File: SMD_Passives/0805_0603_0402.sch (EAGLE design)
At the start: 5 parts

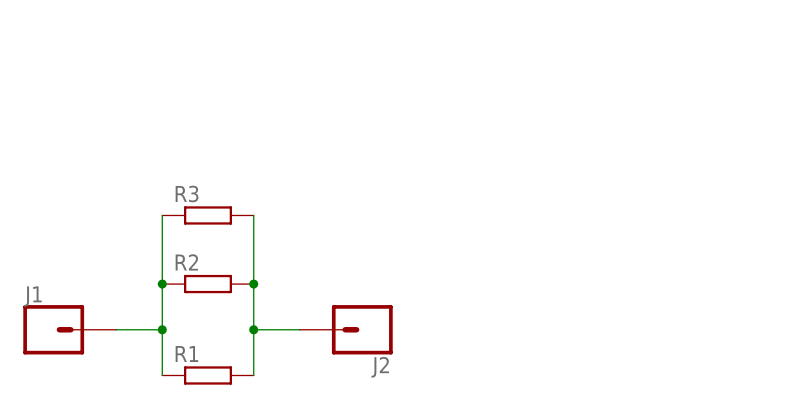
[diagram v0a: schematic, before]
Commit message: Updated passive SMD breakout boards to meet PCB specs
JLC PCB requires a 5x5mm minimum size, and the single SMD adapters were too small for this, so converted to make them wide enough, and made them "dual" to maximize the spaced used
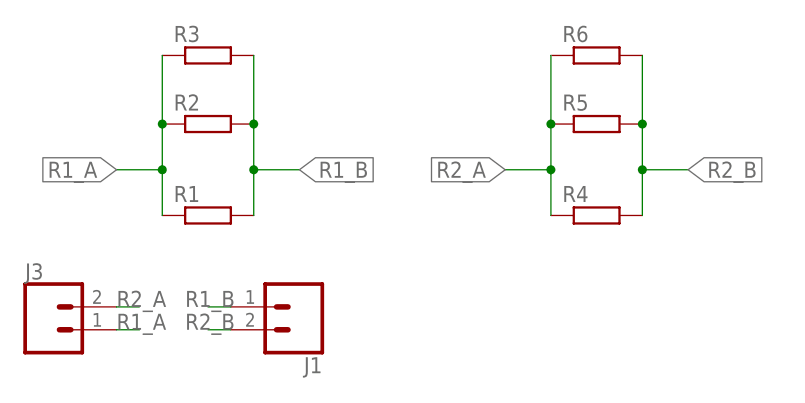
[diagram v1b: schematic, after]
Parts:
- removed J2: (no value), bschulz:CONN_01
- added J3: (no value), bschulz:CONN_02
- added R4: (no value), bschulz_passives:R-EU_R0805
- added R5: (no value), bschulz_passives:R-EU_R0603
- added R6: (no value), bschulz_passives:R-EU_R0402
- J1: device bschulz:CONN_01 -> bschulz:CONN_02
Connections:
- removed net N$1: J1.1, R1.1, R2.1, R3.1
- removed net N$2: J2.1, R1.2, R2.2, R3.2
- new net R1_A: J3.1, R1.1, R2.1, R3.1
- new net R1_B: J1.1, R1.2, R2.2, R3.2
- new net R2_A: J3.2, R4.1, R5.1, R6.1
- new net R2_B: J1.2, R4.2, R5.2, R6.2
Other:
- moved on the sheet: R1, R2, R3
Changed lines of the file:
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@@
 <part name="R1" library="bschulz_passives" deviceset="R-EU_" device="R0805"/>
 <part name="R2" library="bschulz_passives" deviceset="R-EU_" device="R0603"/>
-<part name="J1" library="bschulz" deviceset="CONN_01" device="" package3d_urn="urn:adsk.eagle:package:38028/1"/>
-<part name="J2" library="bschulz" deviceset="CONN_01" device="" package3d_urn="urn:adsk.eagle:package:38028/1"/>
 <part name="R3" library="bschulz_passives" deviceset="R-EU_" device="R0402"/>
+<part name="J3" library="bschulz" deviceset="CONN_02" device=""/>
+<part name="J1" library="bschulz" deviceset="CONN_02" device=""/>
+<part name="R4" library="bschulz_passives" deviceset="R-EU_" device="R0805"/>
+<part name="R5" library="bschulz_passives" deviceset="R-EU_" device="R0603"/>
+<part name="R6" library="bschulz_passives" deviceset="R-EU_" device="R0402"/>
 </parts>
 <sheets>
@@
 </plain>
 <instances>
-<instance part="R1" gate="G$1" x="25.4" y="7.62" smashed="yes">
-<attribute name="NAME" x="21.59" y="9.1186" size="1.778" layer="95"/>
-<attribute name="VALUE" x="21.59" y="4.318" size="1.778" layer="96"/>
-</instance>
-<instance part="R2" gate="G$1" x="25.4" y="17.78" smashed="yes">
-<attribute name="NAME" x="21.59" y="19.2786" size="1.778" layer="95"/>
-<attribute name="VALUE" x="21.59" y="14.478" size="1.778" layer="96"/>
-</instance>
-<instance part="J1" gate="G$1" x="7.62" y="12.7" smashed="yes">
-<attribute name="VALUE" x="5.08" y="7.874" size="1.778" layer="96" font="vector"/>
-<attribute name="NAME" x="5.08" y="15.748" size="1.778" layer="95" font="vector"/>
-</instance>
-<instance part="J2" gate="G$1" x="43.18" y="12.7" smashed="yes" rot="R180">
-<attribute name="VALUE" x="45.72" y="17.526" size="1.778" layer="96" font="vector" rot="R180"/>
-<attribute name="NAME" x="45.72" y="9.652" size="1.778" layer="95" font="vector" rot="R180"/>
-</instance>
-<instance part="R3" gate="G$1" x="25.4" y="25.4" smashed="yes">
+<instance part="R1" gate="G$1" x="25.4" y="25.4" smashed="yes">
 <attribute name="NAME" x="21.59" y="26.8986" size="1.778" layer="95"/>
 <attribute name="VALUE" x="21.59" y="22.098" size="1.778" layer="96"/>
+</instance>
+<instance part="R2" gate="G$1" x="25.4" y="35.56" smashed="yes">
+<attribute name="NAME" x="21.59" y="37.0586" size="1.778" layer="95"/>
+<attribute name="VALUE" x="21.59" y="32.258" size="1.778" layer="96"/>
+</instance>
+<instance part="R3" gate="G$1" x="25.4" y="43.18" smashed="yes">
+<attribute name="NAME" x="21.59" y="44.6786" size="1.778" layer="95"/>
+<attribute name="VALUE" x="21.59" y="39.878" size="1.778" layer="96"/>
+</instance>
+<instance part="J3" gate="G$1" x="7.62" y="12.7" smashed="yes">
+<attribute name="VALUE" x="5.08" y="7.874" size="1.778" layer="96" font="vector"/>
+<attribute name="NAME" x="5.08" y="18.288" size="1.778" layer="95" font="vector"/>
+</instance>
+<instance part="J1" gate="G$1" x="35.56" y="15.24" smashed="yes" rot="R180">
+<attribute name="VALUE" x="38.1" y="20.066" size="1.778" layer="96" font="vector" rot="R180"/>
+<attribute name="NAME" x="38.1" y="9.652" size="1.778" layer="95" font="vector" rot="R180"/>
+</instance>
+<instance part="R4" gate="G$1" x="68.58" y="25.4" smashed="yes">
+<attribute name="NAME" x="64.77" y="26.8986" size="1.778" layer="95"/>
+<attribute name="VALUE" x="64.77" y="22.098" size="1.778" layer="96"/>
+</instance>
+<instance part="R5" gate="G$1" x="68.58" y="35.56" smashed="yes">
+<attribute name="NAME" x="64.77" y="37.0586" size="1.778" layer="95"/>
+<attribute name="VALUE" x="64.77" y="32.258" size="1.778" layer="96"/>
+</instance>
+<instance part="R6" gate="G$1" x="68.58" y="43.18" smashed="yes">
+<attribute name="NAME" x="64.77" y="44.6786" size="1.778" layer="95"/>
+<attribute name="VALUE" x="64.77" y="39.878" size="1.778" layer="96"/>
 </instance>
 </instances>
@@
 </busses>
 <nets>
-<net name="N$1" class="0">
+<net name="R2_A" class="0">
+<segment>
+<pinref part="J3" gate="G$1" pin="2"/>
+<wire x1="15.24" y1="15.24" x2="17.78" y2="15.24" width="0.1524" layer="91"/>
+<label x="15.24" y="15.24" size="1.778" layer="95"/>
+</segment>
+<segment>
+<pinref part="R4" gate="G$1" pin="1"/>
+<pinref part="R5" gate="G$1" pin="1"/>
+<wire x1="63.5" y1="25.4" x2="63.5" y2="30.48" width="0.1524" layer="91"/>
+<pinref part="R6" gate="G$1" pin="1"/>
+<wire x1="63.5" y1="30.48" x2="63.5" y2="35.56" width="0.1524" layer="91"/>
+<wire x1="63.5" y1="35.56" x2="63.5" y2="43.18" width="0.1524" layer="91"/>
+<junction x="63.5" y="35.56"/>
+<wire x1="63.5" y1="30.48" x2="58.42" y2="30.48" width="0.1524" layer="91"/>
+<junction x="63.5" y="30.48"/>
+<label x="58.42" y="30.48" size="1.778" layer="95" rot="R180" xref="yes"/>
+</segment>
+</net>
+<net name="R2_B" class="0">
+<segment>
+<pinref part="R5" gate="G$1" pin="2"/>
+<pinref part="R4" gate="G$1" pin="2"/>
+<wire x1="73.66" y1="35.56" x2="73.66" y2="30.48" width="0.1524" layer="91"/>
+<wire x1="73.66" y1="30.48" x2="73.66" y2="25.4" width="0.1524" layer="91"/>
+<wire x1="78.74" y1="30.48" x2="73.66" y2="30.48" width="0.1524" layer="91"/>
+<junction x="73.66" y="30.48"/>
+<pinref part="R6" gate="G$1" pin="2"/>
+<wire x1="73.66" y1="43.18" x2="73.66" y2="35.56" width="0.1524" layer="91"/>
+<junction x="73.66" y="35.56"/>
+<label x="78.74" y="30.48" size="1.778" layer="95" xref="yes"/>
+</segment>
+<segment>
+<pinref part="J1" gate="G$1" pin="2"/>
+<wire x1="27.94" y1="12.7" x2="25.4" y2="12.7" width="0.1524" layer="91"/>
+<label x="22.86" y="12.7" size="1.778" layer="95"/>
+</segment>
+</net>
+<net name="R1_A" class="0">
+<segment>
+<pinref part="J3" gate="G$1" pin="1"/>
+<wire x1="15.24" y1="12.7" x2="17.78" y2="12.7" width="0.1524" layer="91"/>
+<label x="15.24" y="12.7" size="1.778" layer="95"/>
+</segment>
 <segment>
 <pinref part="R1" gate="G$1" pin="1"/>
 <pinref part="R2" gate="G$1" pin="1"/>
-<wire x1="20.32" y1="7.62" x2="20.32" y2="12.7" width="0.1524" layer="91"/>
-<pinref part="J1" gate="G$1" pin="1"/>
-<wire x1="20.32" y1="12.7" x2="20.32" y2="17.78" width="0.1524" layer="91"/>
-<wire x1="15.24" y1="12.7" x2="20.32" y2="12.7" width="0.1524" layer="91"/>
-<junction x="20.32" y="12.7"/>
+<wire x1="20.32" y1="25.4" x2="20.32" y2="30.48" width="0.1524" layer="91"/>
 <pinref part="R3" gate="G$1" pin="1"/>
-<wire x1="20.32" y1="17.78" x2="20.32" y2="25.4" width="0.1524" layer="91"/>
-<junction x="20.32" y="17.78"/>
+<wire x1="20.32" y1="30.48" x2="20.32" y2="35.56" width="0.1524" layer="91"/>
+<wire x1="20.32" y1="35.56" x2="20.32" y2="43.18" width="0.1524" layer="91"/>
+<junction x="20.32" y="35.56"/>
+<wire x1="20.32" y1="30.48" x2="15.24" y2="30.48" width="0.1524" layer="91"/>
+<junction x="20.32" y="30.48"/>
+<label x="15.24" y="30.48" size="1.778" layer="95" rot="R180" xref="yes"/>
 </segment>
 </net>
-<net name="N$2" class="0">
+<net name="R1_B" class="0">
 <segment>
 <pinref part="R2" gate="G$1" pin="2"/>
 <pinref part="R1" gate="G$1" pin="2"/>
-<wire x1="30.48" y1="17.78" x2="30.48" y2="12.7" width="0.1524" layer="91"/>
-<pinref part="J2" gate="G$1" pin="1"/>
-<wire x1="30.48" y1="12.7" x2="30.48" y2="7.62" width="0.1524" layer="91"/>
-<wire x1="35.56" y1="12.7" x2="30.48" y2="12.7" width="0.1524" layer="91"/>
-<junction x="30.48" y="12.7"/>
+<wire x1="30.48" y1="35.56" x2="30.48" y2="30.48" width="0.1524" layer="91"/>
+<wire x1="30.48" y1="30.48" x2="30.48" y2="25.4" width="0.1524" layer="91"/>
+<wire x1="35.56" y1="30.48" x2="30.48" y2="30.48" width="0.1524" layer="91"/>
+<junction x="30.48" y="30.48"/>
 <pinref part="R3" gate="G$1" pin="2"/>
-<wire x1="30.48" y1="25.4" x2="30.48" y2="17.78" width="0.1524" layer="91"/>
-<junction x="30.48" y="17.78"/>
+<wire x1="30.48" y1="43.18" x2="30.48" y2="35.56" width="0.1524" layer="91"/>
+<junction x="30.48" y="35.56"/>
+<label x="35.56" y="30.48" size="1.778" layer="95" xref="yes"/>
+</segment>
+<segment>
+<pinref part="J1" gate="G$1" pin="1"/>
+<wire x1="27.94" y1="15.24" x2="25.4" y2="15.24" width="0.1524" layer="91"/>
+<label x="22.86" y="15.24" size="1.778" layer="95"/>
 </segment>
 </net>
@@
 </schematic>
 </drawing>
-<compatibility>
-<note version="8.3" severity="warning">
-Since Version 8.3, EAGLE supports URNs for individual library
-assets (packages, symbols, and devices). The URNs of those assets
-will not be understood (or retained) with this version.
-</note>
-<note version="8.3" severity="warning">
-Since Version 8.3, EAGLE supports the association of 3D packages
-with devices in libraries, schematics, and board files. Those 3D
-packages will not be understood (or retained) with this version.
-</note>
-</compatibility>
 </eagle>
